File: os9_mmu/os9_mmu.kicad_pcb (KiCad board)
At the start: 2 copper layers, 86.4 x 93.3 mm, 18 parts, among them U1 74LS257, U2 74LS157, U3 74LS273, U4 74LS04, U5 74LS02, U6 6809E

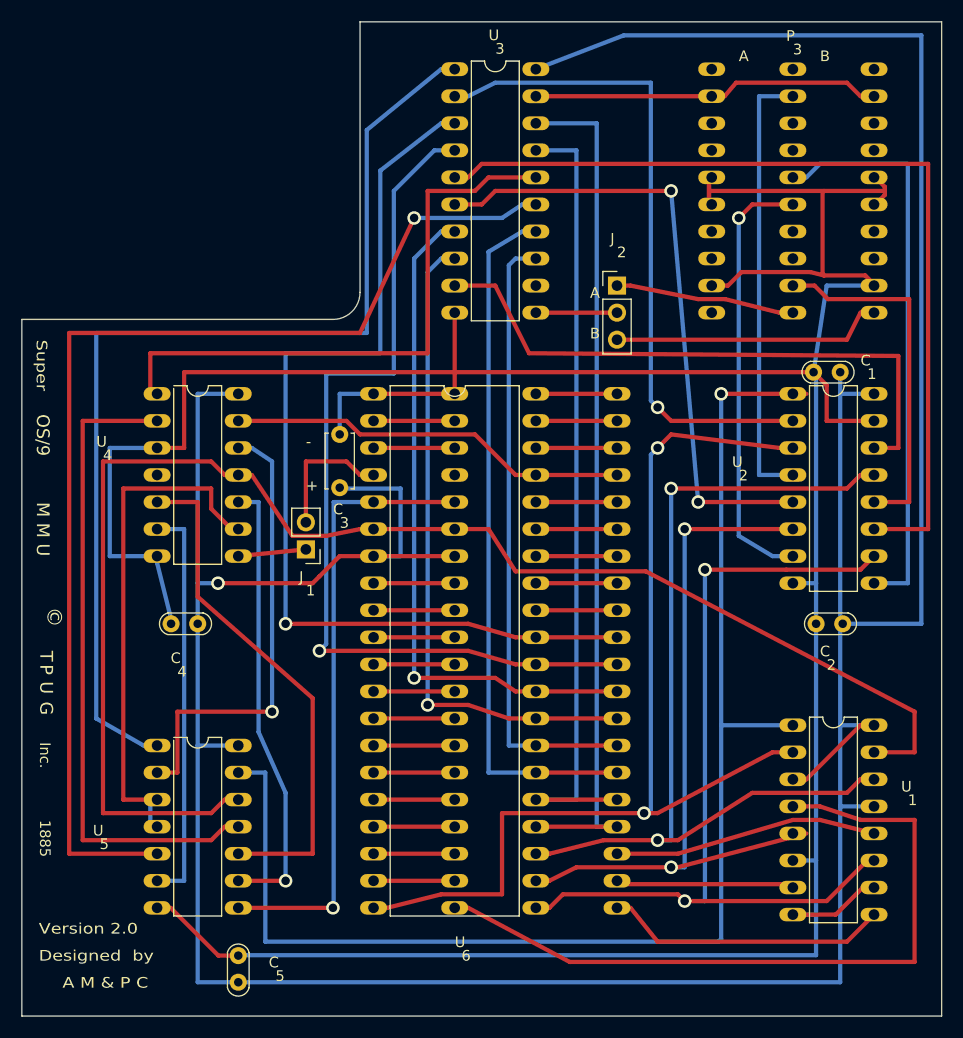
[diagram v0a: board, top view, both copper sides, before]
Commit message: MMU adjustments
-adjusted power trace widths
-reintroduced solder mask layer - was absence to give board a vintage look but makes silkscreen prints impossible
-fixed license links in drawing sheets to match board prints, readme and project
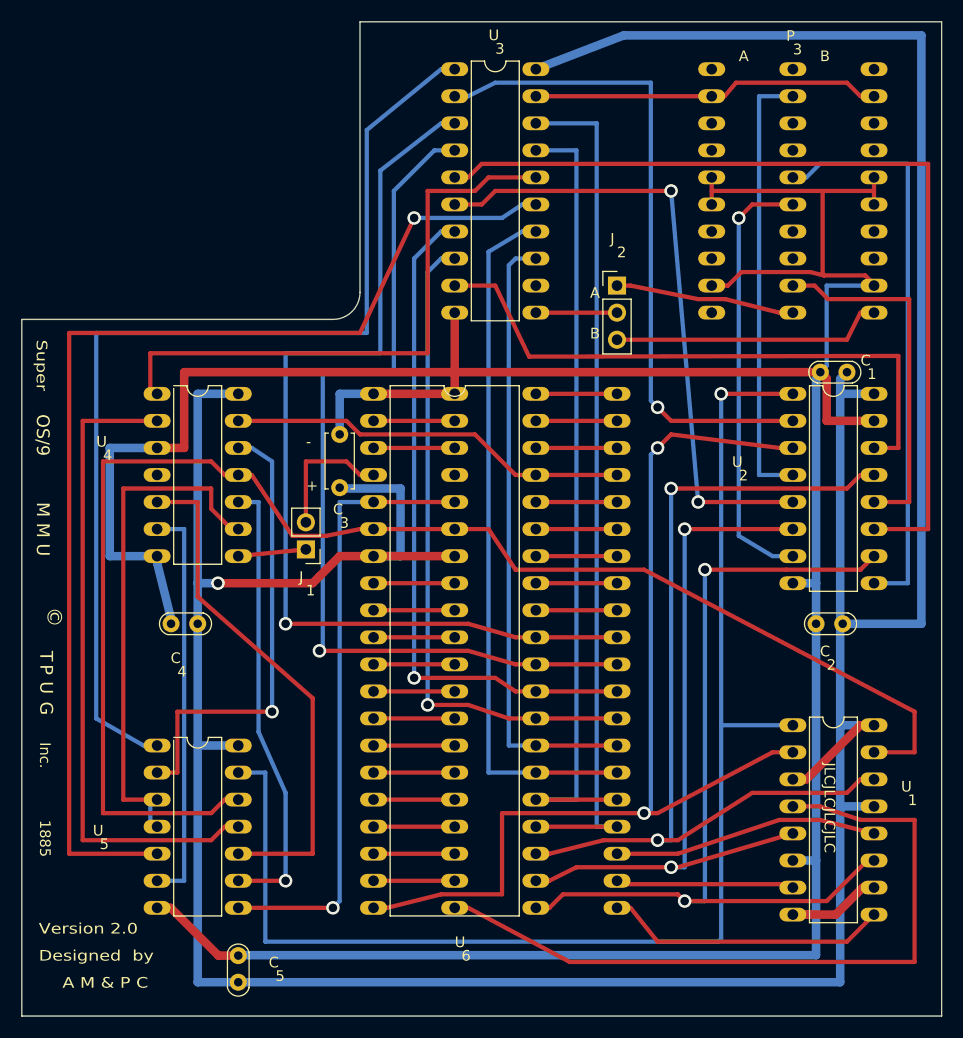
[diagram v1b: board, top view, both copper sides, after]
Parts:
- moved C1 0.63 mm to (176.5, 71.6)
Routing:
- net GND: track 323.3 -> 317.2 mm
- net Net-(U1-S): track 127.2 -> 126.0 mm
- net /BANK1: track 83.1 -> 84.3 mm
- net A14_{MMU}: track 69.3 -> 68.1 mm
- net BA: track 137.8 -> 139.0 mm
- net /BANK3: track 56.2 -> 56.8 mm
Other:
- board text added: "JLCJLCJLCJLC"
